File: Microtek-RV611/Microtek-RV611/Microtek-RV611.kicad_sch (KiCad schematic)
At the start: 19 parts, among them P1 Bus_Apple_II_Card_Side, P2 Conn_02x13_Odd_Even, Q1 2N3906, Q2 2N3906, U1 74LS00, U2 74LS74, U3 74298, U4 TBP28L22N, U5 74LS174

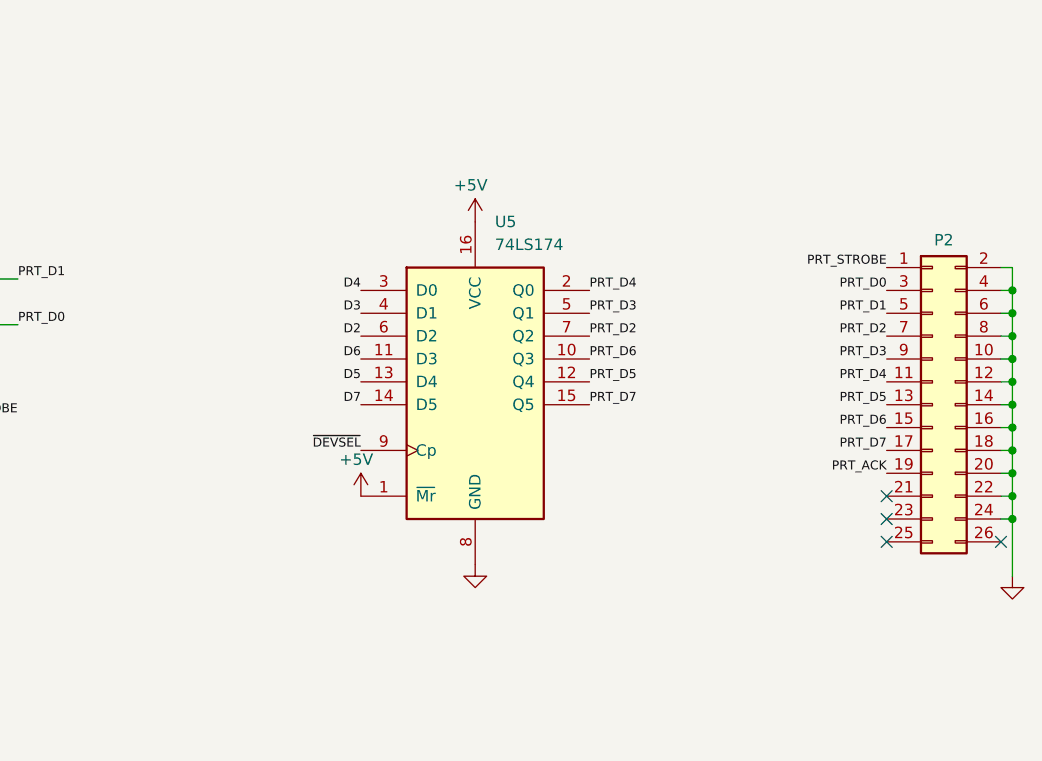
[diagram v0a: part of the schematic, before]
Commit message: RV611: Fix typo in the schematic title and add the missing ROM contents
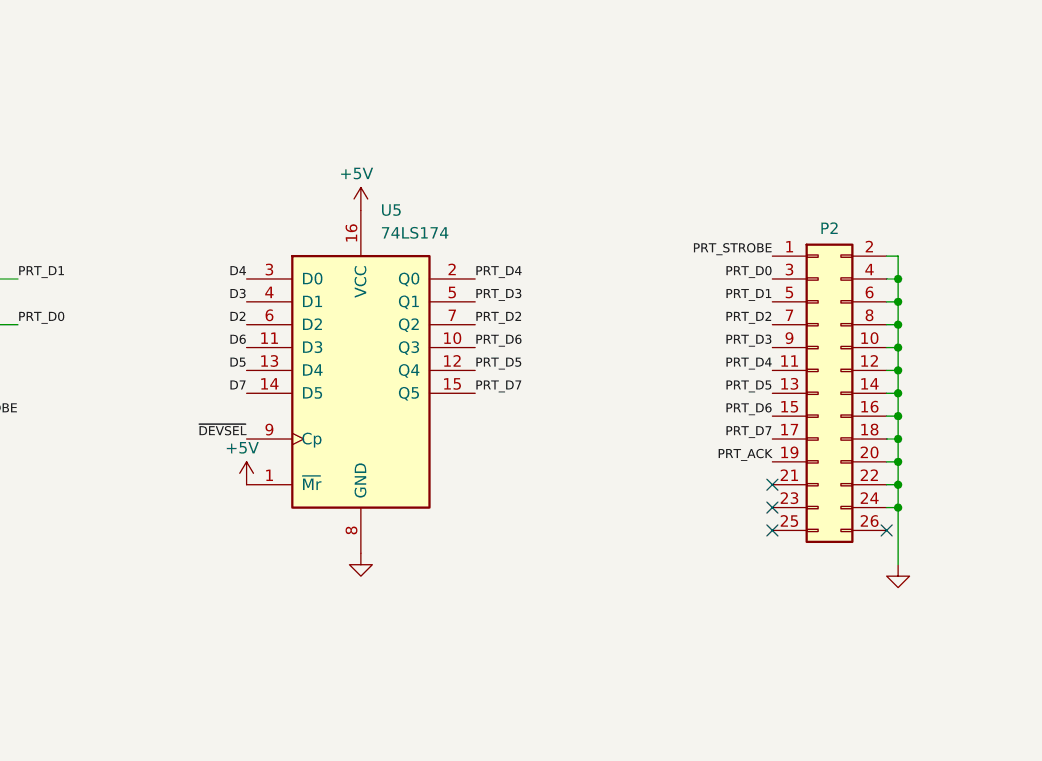
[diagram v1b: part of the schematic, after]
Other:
- title: Microtek PV611 -> Microtek RV611
- moved on the sheet: P2, U5
